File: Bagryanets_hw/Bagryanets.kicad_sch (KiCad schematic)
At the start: 102 parts, among them U1 SX1276

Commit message: Added STL
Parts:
- added H1, H2, H3, H4: MountingHole, Kais_Lib:Hole_2.4, symbol Mechanical:MountingHole
- added R22: *, Resistors:RES_0603, symbol Device:R
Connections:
- net +3V3: now also R22.2
- net at C31.2, DD1.7 (NRST), SB2.2: now also R22.1
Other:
- moved on the sheet: C31
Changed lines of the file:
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@@
   (junction (at 383.54 53.34) (diameter 0) (color 0 0 0 0)
   )
+  (junction (at 224.79 173.99) (diameter 0) (color 0 0 0 0)
+  )
   (junction (at 207.01 191.77) (diameter 0) (color 0 0 0 0)
   )
@@
     (stroke (width 0) (type default))
   )
+  (wire (pts (xy 224.79 161.29) (xy 224.79 163.83))
+    (stroke (width 0) (type default))
+  )
   (wire (pts (xy 200.66 76.2) (xy 201.93 76.2))
     (stroke (width 0) (type default))
@@
     (stroke (width 0) (type default))
   )
+  (wire (pts (xy 224.79 171.45) (xy 224.79 173.99))
+    (stroke (width 0) (type default))
+  )
   (wire (pts (xy 382.27 53.34) (xy 383.54 53.34))
     (stroke (width 0) (type default))
@@
     (stroke (width 0) (type default))
   )
-  (wire (pts (xy 237.49 173.99) (xy 237.49 175.26))
+  (wire (pts (xy 237.49 173.99) (xy 237.49 176.53))
     (stroke (width 0) (type default))
   )
@@
     (stroke (width 0) (type default))
   )
-  (wire (pts (xy 237.49 182.88) (xy 237.49 185.42))
+  (wire (pts (xy 237.49 184.15) (xy 237.49 185.42))
     (stroke (width 0) (type default))
   )
@@
     (effects (font (size 1.27 1.27)) (justify left bottom))
   )
-  (text "Конденсатор\nрекомендуется по даташиту" (at 224.79 172.72 0)
+  (text "Конденсатор\nрекомендуется по даташиту" (at 228.6 172.72 0)
     (effects (font (size 1.27 1.27)) (justify left bottom))
   )
@@
     (effects (font (size 1.27 1.27)) (justify left bottom))
   )
+  (text "Не паять" (at 215.9 163.83 0)
+    (effects (font (size 1.27 1.27)) (justify left bottom))
+  )
   (text "Не паять" (at 91.44 90.17 0)
     (effects (font (size 1.27 1.27)) (justify left bottom))
@@
     )
   )
+  (symbol (lib_id "Mechanical:MountingHole") (at 196.85 278.13 0) (unit 1)
+    (in_bom yes) (on_board yes) (dnp no) (fields_autoplaced)
+    (property "Reference" "H3" (at 199.39 276.86 0)
+      (effects (font (size 1.27 1.27)) (justify left))
+    )
+    (property "Value" "MountingHole" (at 199.39 279.4 0)
+      (effects (font (size 1.27 1.27)) (justify left))
+    )
+    (property "Footprint" "Kais_Lib:Hole_2.4" (at 196.85 278.13 0)
+      (effects (font (size 1.27 1.27)) hide)
+    )
+    (property "Datasheet" "~" (at 196.85 278.13 0)
+      (effects (font (size 1.27 1.27)) hide)
+    )
+    (instances
+      (project "Bagryanets"
+        (path "/e63e39d7-6ac0-4ffd-8aa3-1841a4541b55"
+          (reference "H3") (unit 1)
+        )
+      )
+    )
+  )
   (symbol (lib_id "#USER:N-Channel MOSFET_GOST") (at 48.26 148.59 270) (mirror x) (unit 1)
     (in_bom yes) (on_board yes) (dnp no)
@@
     )
   )
+  (symbol (lib_id "power:+3.3V") (at 224.79 161.29 0) (unit 1)
+    (in_bom yes) (on_board yes) (dnp no)
+    (property "Reference" "#PWR082" (at 224.79 165.1 0)
+      (effects (font (size 1.27 1.27)) hide)
+    )
+    (property "Value" "+3.3V" (at 228.6 160.02 0)
+      (effects (font (size 1.27 1.27)))
+    )
+    (property "Footprint" "" (at 224.79 161.29 0)
+      (effects (font (size 1.27 1.27)) hide)
+    )
+    (property "Datasheet" "" (at 224.79 161.29 0)
+      (effects (font (size 1.27 1.27)) hide)
+    )
+    (pin "1")
+    (instances
+      (project "Bagryanets"
+        (path "/e63e39d7-6ac0-4ffd-8aa3-1841a4541b55"
+          (reference "#PWR082") (unit 1)
+        )
+      )
+    )
+  )
   (symbol (lib_id "#USER:GND_GOST") (at 193.04 151.13 0) (unit 1)
     (in_bom yes) (on_board yes) (dnp no) (fields_autoplaced)
@@
     )
   )
+  (symbol (lib_id "Mechanical:MountingHole") (at 196.85 283.21 0) (unit 1)
+    (in_bom yes) (on_board yes) (dnp no) (fields_autoplaced)
+    (property "Reference" "H4" (at 199.39 281.94 0)
+      (effects (font (size 1.27 1.27)) (justify left))
+    )
+    (property "Value" "MountingHole" (at 199.39 284.48 0)
+      (effects (font (size 1.27 1.27)) (justify left))
+    )
+    (property "Footprint" "Kais_Lib:Hole_2.4" (at 196.85 283.21 0)
+      (effects (font (size 1.27 1.27)) hide)
+    )
+    (property "Datasheet" "~" (at 196.85 283.21 0)
+      (effects (font (size 1.27 1.27)) hide)
+    )
+    (instances
+      (project "Bagryanets"
+        (path "/e63e39d7-6ac0-4ffd-8aa3-1841a4541b55"
+          (reference "H4") (unit 1)
+        )
+      )
+    )
+  )
   (symbol (lib_id "#USER:GND_GOST") (at 63.5 265.43 0) (unit 1)
     (in_bom yes) (on_board yes) (dnp no) (fields_autoplaced)
@@
     )
   )
+  (symbol (lib_id "Mechanical:MountingHole") (at 196.85 273.05 0) (unit 1)
+    (in_bom yes) (on_board yes) (dnp no) (fields_autoplaced)
+    (property "Reference" "H2" (at 199.39 271.78 0)
+      (effects (font (size 1.27 1.27)) (justify left))
+    )
+    (property "Value" "MountingHole" (at 199.39 274.32 0)
+      (effects (font (size 1.27 1.27)) (justify left))
+    )
+    (property "Footprint" "Kais_Lib:Hole_2.4" (at 196.85 273.05 0)
+      (effects (font (size 1.27 1.27)) hide)
+    )
+    (property "Datasheet" "~" (at 196.85 273.05 0)
+      (effects (font (size 1.27 1.27)) hide)
+    )
+    (instances
+      (project "Bagryanets"
+        (path "/e63e39d7-6ac0-4ffd-8aa3-1841a4541b55"
+          (reference "H2") (unit 1)
+        )
+      )
+    )
+  )
   (symbol (lib_id "Device:C") (at 208.28 236.22 180) (unit 1)
     (in_bom yes) (on_board yes) (dnp no)
@@
     )
   )
+  (symbol (lib_id "Mechanical:MountingHole") (at 196.85 267.97 0) (unit 1)
+    (in_bom yes) (on_board yes) (dnp no) (fields_autoplaced)
+    (property "Reference" "H1" (at 199.39 266.7 0)
+      (effects (font (size 1.27 1.27)) (justify left))
+    )
+    (property "Value" "MountingHole" (at 199.39 269.24 0)
+      (effects (font (size 1.27 1.27)) (justify left))
+    )
+    (property "Footprint" "Kais_Lib:Hole_2.4" (at 196.85 267.97 0)
+      (effects (font (size 1.27 1.27)) hide)
+    )
+    (property "Datasheet" "~" (at 196.85 267.97 0)
+      (effects (font (size 1.27 1.27)) hide)
+    )
+    (instances
+      (project "Bagryanets"
+        (path "/e63e39d7-6ac0-4ffd-8aa3-1841a4541b55"
+          (reference "H1") (unit 1)
+        )
+      )
+    )
+  )
   (symbol (lib_id "Device:L") (at 302.26 45.72 90) (unit 1)
     (in_bom yes) (on_board yes) (dnp no)
@@
     )
   )
-  (symbol (lib_id "Device:C") (at 237.49 179.07 180) (unit 1)
+  (symbol (lib_id "Device:C") (at 237.49 180.34 180) (unit 1)
     (in_bom yes) (on_board yes) (dnp no)
-    (property "Reference" "C31" (at 245.11 177.8 0)
+    (property "Reference" "C31" (at 245.11 179.07 0)
       (effects (font (size 1.27 1.27)) (justify left))
     )
-    (property "Value" "100n" (at 245.11 180.34 0)
+    (property "Value" "100n" (at 245.11 181.61 0)
       (effects (font (size 1.27 1.27)) (justify left))
     )
-    (property "Footprint" "Capacitors:CAP_0402" (at 236.5248 175.26 0)
+    (property "Footprint" "Capacitors:CAP_0402" (at 236.5248 176.53 0)
       (effects (font (size 1.27 1.27)) hide)
     )
-    (property "Datasheet" "~" (at 237.49 179.07 0)
+    (property "Datasheet" "~" (at 237.49 180.34 0)
       (effects (font (size 1.27 1.27)) hide)
     )
@@
         )
       )
+    )
+  )
+  (symbol (lib_id "Device:R") (at 224.79 167.64 180) (unit 1)
+    (in_bom yes) (on_board yes) (dnp no)
+    (property "Reference" "R22" (at 218.44 166.3699 0)
+      (effects (font (size 1.27 1.27)) (justify right))
+    )
+    (property "Value" "*" (at 220.98 168.9099 0)
+      (effects (font (size 1.27 1.27)) (justify right))
+    )
+    (property "Footprint" "Resistors:RES_0603" (at 226.568 167.64 90)
+      (effects (font (size 1.27 1.27)) hide)
+    )
+    (property "Datasheet" "~" (at 224.79 167.64 0)
+      (effects (font (size 1.27 1.27)) hide)
+    )
+    (pin "1")
+    (pin "2")
+    (instances
+      (project "Bagryanets"
+        (path "/e63e39d7-6ac0-4ffd-8aa3-1841a4541b55"
+          (reference "R22") (unit 1)
+        )
+      )

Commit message: Added bom, small schematic changes
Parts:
- removed C1: 100n, Capacitors:CAP_0402, symbol Device:C
- removed R2, R3: 100k, Resistors:RES_0603, symbol Device:R
- added C8: 100n, Capacitors:CAP_0402, symbol Device:C
- added R6, R7: 100k, Resistors:RES_0603, symbol Device:R
- added TP1, TP2, TP3, TP4, TP5, TP6, TP7, TP8, TP9: TestPoint, PCB:TESTPOINT_1MM, symbol Connector:TestPoint
- C11: renamed from C10; now not fitted
- C12: renamed from C11; now not fitted
- C14, C19, C24: value 10p -> 8p
- C18, C23: value 12.5p -> 9p
- C45, C46, L8: now not fitted
- C9: renamed from C12; value 10p -> 8p
- H1, H2, H3, H4: footprint Kais_Lib:Hole_2.4 -> MountingHole:MountingHole_2.5mm
- R22: renamed from R21; value 200 -> 510
- R4: renamed from R6; now not fitted
- R5: renamed from R7; now not fitted
- renumbered C2 to C1, C9 to C10, C3 to C2, C4 to C3, C5 to C4, C6 to C5, C7 to C6, C8 to C7, R22 to R16, R16 to R17, R17 to R18, R18 to R19, R4 to R2, R19 to R20, R20 to R21, R5 to R3
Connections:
- net BatCtrl: now also C8.2, R6.1, R7.2
- net Battery: now also R6.2
- net GND: now also C8.1, R7.1
- net IR_IN1: now also TP2.1
- net IR_IN2: now also TP1.1
- net L.DIO0: now also TP3.1
- net L.DIO1: now also TP4.1
- net L.MISO: now also TP6.1
- net L.MOSI: now also TP7.1
- net L.NSS: now also TP8.1
- net L.RESET: now also TP9.1
- net L.SCK: now also TP5.1
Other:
- note added: "80mA - max"
- note added: "TIM15/TIM2 - формирует частоту пачек для TIM1 - внутреннее соединение Заполнение пачек - ИК выход TIM1: 1 - PA8 2 - PA9 3 - PA10 4 - PA11"
- note removed: "TIM15 - формирует частоту пачек для TIM1 - внутреннее соединение Заполнение пачек - ИК выход TIM1: 1 - PA8 2 - PA9 3 - PA10 4 - PA11"
- note removed: "VF=1.5 I=15m"
- moved on the sheet: C14, C9, ZQ1

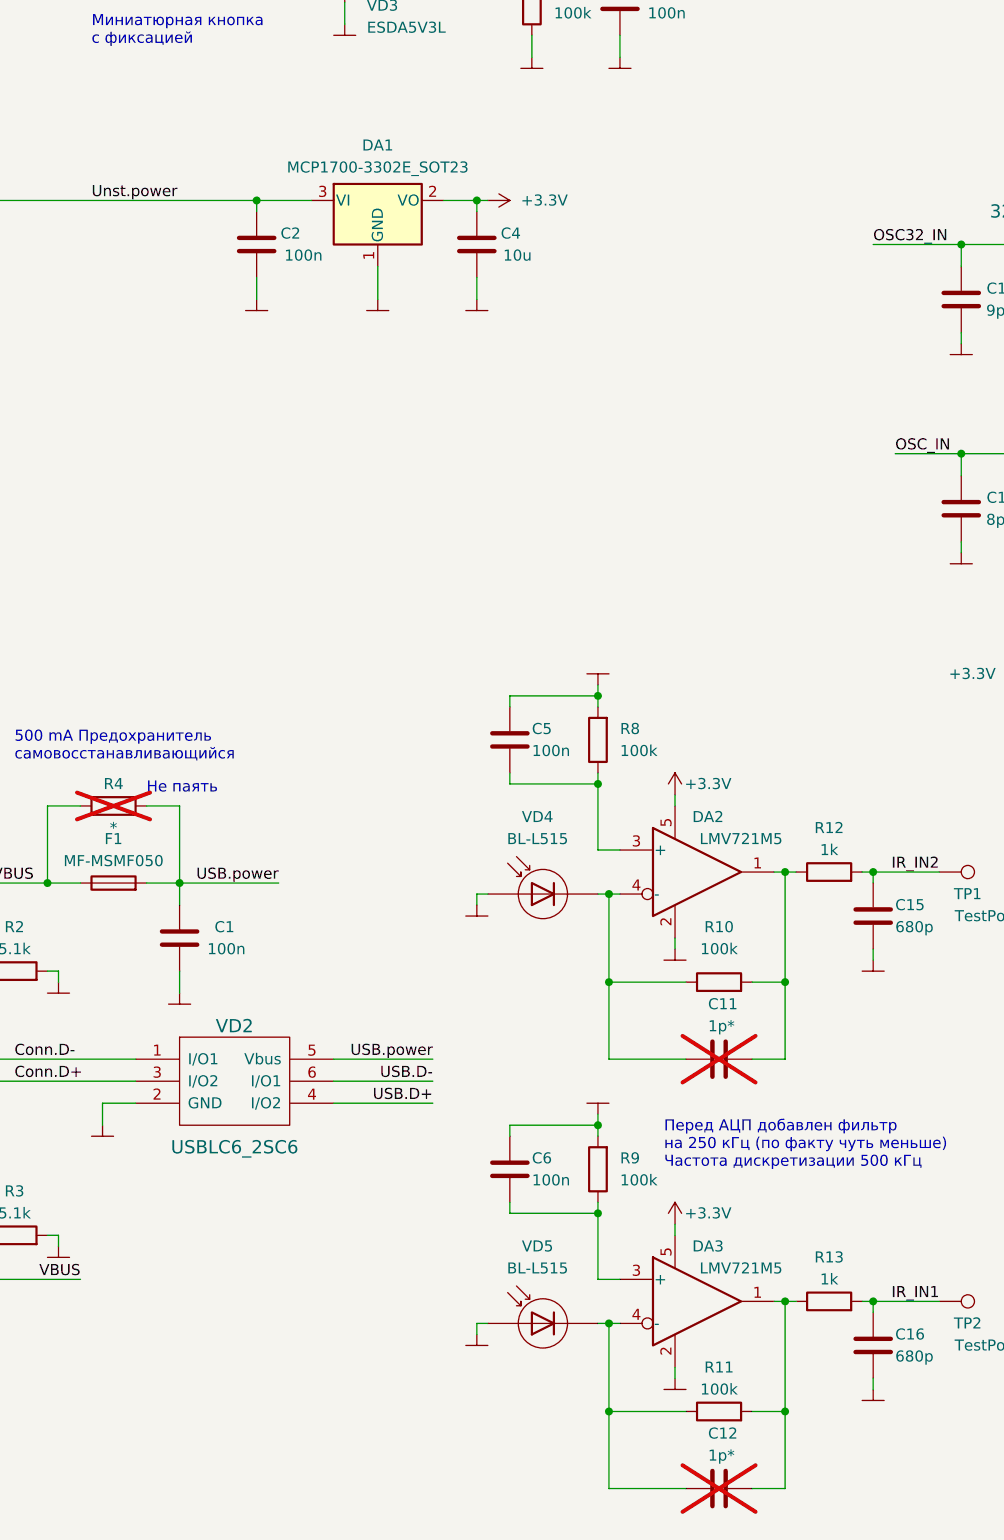
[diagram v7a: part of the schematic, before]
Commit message: Schematic update, IR amplifier working
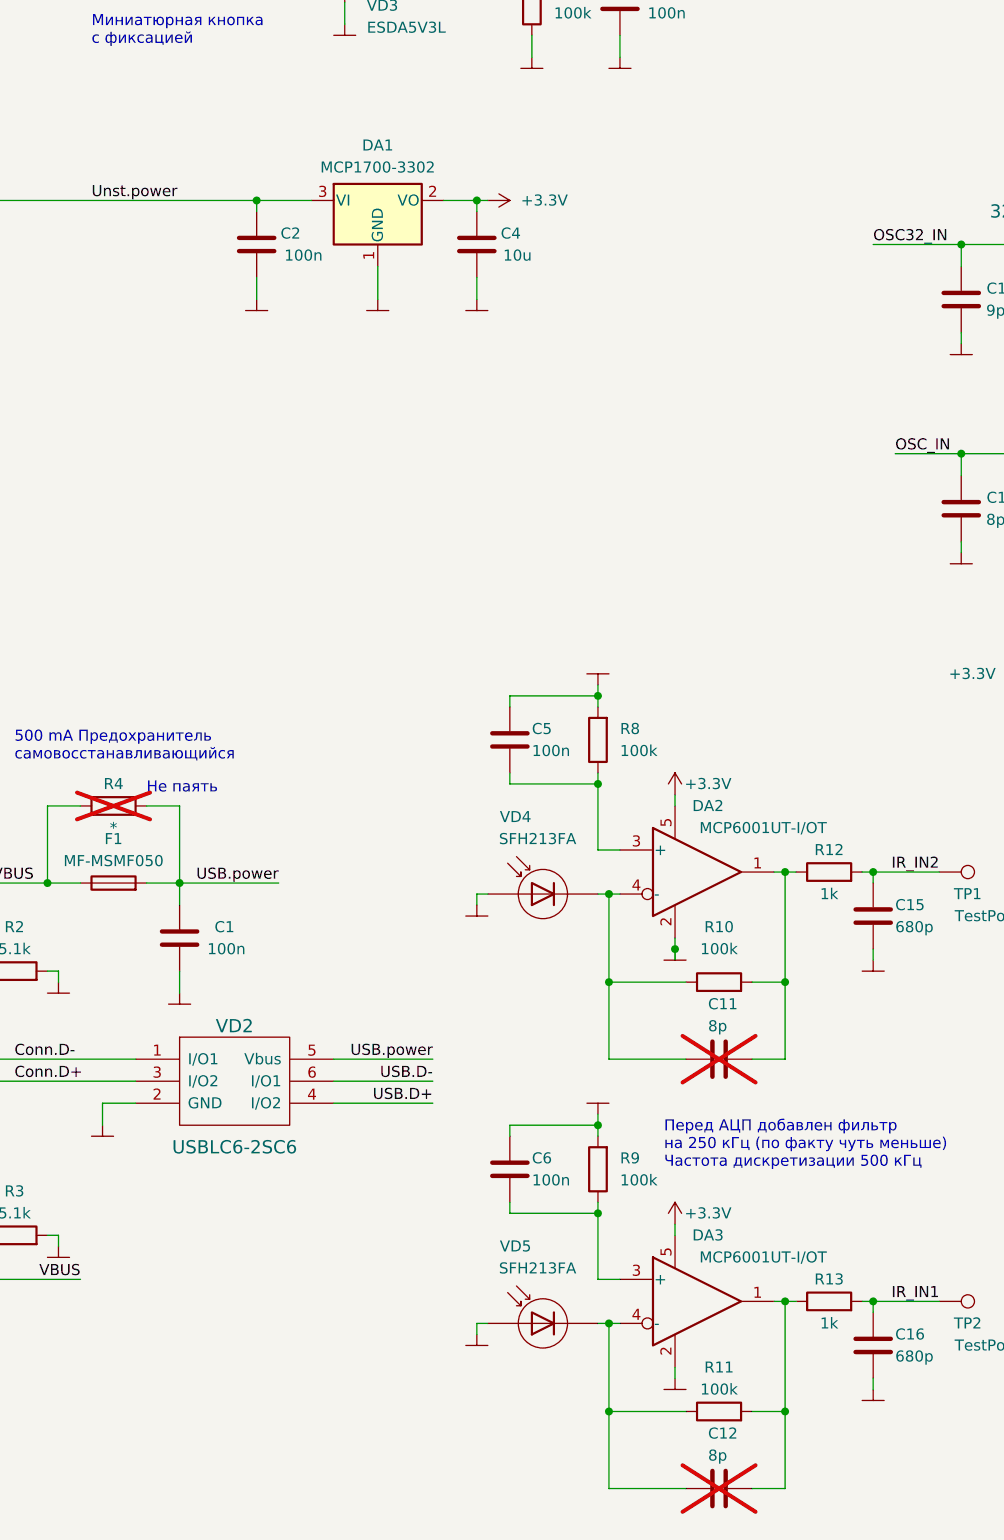
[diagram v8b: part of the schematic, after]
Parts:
- C11, C12: value 1p* -> 8p
- DA1: value MCP1700-3302E_SOT23 -> MCP1700-3302
- DA2, DA3: value LMV721M5 -> MCP6001UT-I/OT
- VD2: value USBLC6_2SC6 -> USBLC6-2SC6
- VD4, VD5: value BL-L515 -> SFH213FA
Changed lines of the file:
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@@
   (junction (at 255.27 38.1) (diameter 0) (color 0 0 0 0)
   )
+  (junction (at 144.78 220.98) (diameter 0) (color 0 0 0 0)
+  )
   (junction (at 55.88 134.62) (diameter 0) (color 0 0 0 0)
   )
@@
     (stroke (width 0) (type default))
   )
+  (wire (pts (xy 156.21 212.09) (xy 157.48 212.09))
+    (stroke (width 0) (type default))
+  )
   (wire (pts (xy 55.88 134.62) (xy 55.88 146.05))
     (stroke (width 0) (type default))
@@
     (stroke (width 0) (type default))
   )
-  (wire (pts (xy 156.21 212.09) (xy 157.48 212.09))
-    (stroke (width 0) (type default))
-  )
   (wire (pts (xy 157.48 212.09) (xy 157.48 224.79))
     (stroke (width 0) (type default))
@@
     (stroke (width 0) (type default))
   )
+  (wire (pts (xy 144.78 222.25) (xy 144.78 220.98))
+    (stroke (width 0) (type default))
+  )
   (wire (pts (xy 97.79 91.44) (xy 97.79 96.52))
     (stroke (width 0) (type default))
@@
   )
   (symbol (lib_id "#USER:D_Photo") (at 129.54 214.63 0) (mirror y) (unit 1)
-    (in_bom yes) (on_board yes) (dnp no) (fields_autoplaced)
-    (property "Reference" "VD4" (at 128.9279 205.74 0)
+    (in_bom yes) (on_board yes) (dnp no)
+    (property "Reference" "VD4" (at 126.3879 205.74 0)
       (effects (font (size 1.27 1.27)))
     )
-    (property "Value" "BL-L515" (at 128.9279 208.28 0)
+    (property "Value" "SFH213FA" (at 128.9279 208.28 0)
       (effects (font (size 1.27 1.27)))
     )
@@
   (symbol (lib_id "Device:R") (at 162.56 261.62 90) (unit 1)
     (in_bom yes) (on_board yes) (dnp no)
-    (property "Reference" "R13" (at 162.56 256.54 90)
+    (property "Reference" "R13" (at 162.56 259.08 90)
       (effects (font (size 1.27 1.27)))
     )
-    (property "Value" "1k" (at 162.56 259.08 90)
+    (property "Value" "1k" (at 162.56 264.16 90)
       (effects (font (size 1.27 1.27)))
     )
@@
   )
   (symbol (lib_id "#USER:D_Photo") (at 129.54 264.16 0) (mirror y) (unit 1)
-    (in_bom yes) (on_board yes) (dnp no) (fields_autoplaced)
-    (property "Reference" "VD5" (at 128.9279 255.27 0)
+    (in_bom yes) (on_board yes) (dnp no)
+    (property "Reference" "VD5" (at 126.3879 255.27 0)
       (effects (font (size 1.27 1.27)))
     )
-    (property "Value" "BL-L515" (at 128.9279 257.81 0)
+    (property "Value" "SFH213FA" (at 128.9279 257.81 0)
       (effects (font (size 1.27 1.27)))
     )
@@
       (effects (font (size 1.27 1.27)) (justify left))
     )
-    (property "Value" "1p*" (at 148.59 279.4 90)
+    (property "Value" "8p" (at 148.59 279.4 90)
       (effects (font (size 1.27 1.27)) (justify left))
     )
@@
       (effects (font (size 1.27 1.27)) (justify left))
     )
-    (property "Value" "1p*" (at 148.59 229.87 90)
+    (property "Value" "8p" (at 148.59 229.87 90)
       (effects (font (size 1.27 1.27)) (justify left))
     )
@@
       (effects (font (size 1.27 1.27)))
     )
-    (property "Value" "MCP1700-3302E_SOT23" (at 110.49 130.81 0)
+    (property "Value" "MCP1700-3302" (at 110.49 130.81 0)
       (effects (font (size 1.27 1.27)))
     )
@@
   (symbol (lib_name "LMV721M5_1") (lib_id "#USER:LMV721M5") (at 147.32 212.09 0) (unit 1)
     (in_bom yes) (on_board yes) (dnp no)
-    (property "Reference" "DA2" (at 148.59 205.74 0)
+    (property "Reference" "DA2" (at 148.59 204.47 0)
       (effects (font (size 1.27 1.27)))
     )
-    (property "Value" "LMV721M5" (at 152.4 208.28 0)
+    (property "Value" "MCP6001UT-I/OT" (at 154.94 207.01 0)
       (effects (font (size 1.27 1.27)))
     )
@@
       (effects (font (size 1.524 1.524)))
     )
-    (property "Value" "USBLC6_2SC6" (at 93.98 243.84 0)
+    (property "Value" "USBLC6-2SC6" (at 93.98 243.84 0)
       (effects (font (size 1.524 1.524)))
     )
@@
   (symbol (lib_id "Device:R") (at 162.56 212.09 90) (unit 1)
     (in_bom yes) (on_board yes) (dnp no)
-    (property "Reference" "R12" (at 162.56 207.01 90)
+    (property "Reference" "R12" (at 162.56 209.55 90)
       (effects (font (size 1.27 1.27)))
     )
-    (property "Value" "1k" (at 162.56 209.55 90)
+    (property "Value" "1k" (at 162.56 214.63 90)
       (effects (font (size 1.27 1.27)))
     )
@@
   (symbol (lib_name "LMV721M5_1") (lib_id "#USER:LMV721M5") (at 147.32 261.62 0) (unit 1)
     (in_bom yes) (on_board yes) (dnp no)
-    (property "Reference" "DA3" (at 148.59 255.27 0)
+    (property "Reference" "DA3" (at 148.59 254 0)
       (effects (font (size 1.27 1.27)))
     )
-    (property "Value" "LMV721M5" (at 152.4 257.81 0)
+    (property "Value" "MCP6001UT-I/OT" (at 154.94 256.54 0)
       (effects (font (size 1.27 1.27)))
     )
